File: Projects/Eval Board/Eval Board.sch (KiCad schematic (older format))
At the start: 34 parts, among them J1 Q OUT, J2 Q OUT, J3 Q OUT, J4 Q OUT, U1 LTC5584

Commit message: Version 2
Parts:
- removed J1: Q OUT, Kevin Library:SAMTEC_SMA-J-P-H-ST-EM1, symbol RandomSMAIFoundOnline:SMA-J-P-H-ST-EM1
- added J3: I Out, AdditionalLibs:SAMTEC_SMA-J-P-H-ST-EM1, symbol RandomSMAIFoundOnline:SMA-J-P-H-ST-EM1
- added J6: Conn_01x02, Connector_PinHeader_1.00mm:PinHeader_1x02_P1.00mm_Vertical, symbol Connector_Generic:Conn_01x02
- added J7: Conn_01x04, Connector_PinHeader_1.00mm:PinHeader_1x04_P1.00mm_Vertical, symbol Connector_Generic:Conn_01x04
- added J8: Conn_01x05, Connector_PinHeader_1.00mm:PinHeader_1x05_P1.00mm_Vertical, symbol Connector_Generic:Conn_01x05
- J1: renamed from J3; value Q OUT -> LO; footprint Kevin Library:SAMTEC_SMA-J-P-H-ST-EM1 -> AdditionalLibs:SAMTEC_SMA-J-P-H-ST-EM1
- J2, J4: footprint Kevin Library:SAMTEC_SMA-J-P-H-ST-EM1 -> AdditionalLibs:SAMTEC_SMA-J-P-H-ST-EM1
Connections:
- net DCOI: now also J8.4 (Pin_4)
- net DCOQ: now also J8.3 (Pin_3)
- net EDC: now also J7.2 (Pin_2)
- net EIP2: now also J7.1 (Pin_1)
- net EN: now also J7.4 (Pin_4)
- net GND: now also J6.2 (Pin_2)
- net IP2Q: now also J8.2 (Pin_2)
- net REF: now also J8.1 (Pin_1)
- net VCC: now also J6.1 (Pin_1)
- net Q-: now reaches J2.2_1, J2.2_2, J2.3_1, J2.3_2, R14.1, U1.20 (Q-)
- net Q+: now reaches J2.1, R13.1, U1.21 (Q+)
- net I+: now reaches R11.1, U1.22 (I-)
- net I+: now also J3.1
- net I-: now reaches R9.1, U1.23 (I+)
- net I-: now also J3.2_1, J3.2_2, J3.3_1, J3.3_2
- net Vbias: now reaches U1.9 (VBias)
- net Vbias: now also J7.3 (Pin_3)
- net RF: now reaches C17.1, J4.1, L6.1
- net LO: now reaches C14.1, J1.1, L5.2
- net IP2I renamed IP21
- net IP21: now also J8.5 (Pin_5)
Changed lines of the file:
@@
 Text GLabel 3100 3250 0    50   Input ~ 0
 REF
-Text GLabel 2600 3650 0    50   Input ~ 0
-IP2Q
-Text GLabel 2600 3750 0    50   Input ~ 0
-DCOQ
-Text GLabel 2600 3850 0    50   Input ~ 0
-DCOI
-Text GLabel 2600 3950 0    50   Input ~ 0
-IP2I
+$Comp
+L power:VCC #PWR0124
+U 1 1 600BE7D0
+P 5200 2350
+F 0 "#PWR0124" H 5200 2200 50  0001 C CNN
+F 1 "VCC" H 5215 2523 50  0000 C CNN
+F 2 "Connector_Pin:Pin_D0.7mm_L6.5mm_W1.8mm_FlatFork" H 5200 2350 50  0001 C CNN
+F 3 "" H 5200 2350 50  0001 C CNN
+	1    5200 2350
+	1    0    0    -1
+$EndComp
+Connection ~ 5200 2350
+Wire Wire Line
+	5200 2350 5600 2350
+$Comp
+L RandomSMAIFoundOnline:SMA-J-P-H-ST-EM1 J1
+U 1 1 600D7F64
+P 9150 4200
+F 0 "J1" H 8990 4286 50  0000 R CNN
+F 1 "LO" H 8990 4195 50  0000 R CNN
+F 2 "AdditionalLibs:SAMTEC_SMA-J-P-H-ST-EM1" H 9150 4200 50  0001 L BNN
+F 3 "" H 9150 4200 50  0001 L BNN
+F 4 "Samtec" H 9150 4200 50  0001 L BNN "MANUFACTURER"
+F 5 "G" H 9150 4200 50  0001 L BNN "PARTREV"
+F 6 "Manufacturer Recommendations" H 9150 4200 50  0001 L BNN "STANDARD"
+F 7 "3.675mm" H 9150 4200 50  0001 L BNN "MAXIMUM_PACKAGE_HEIGHT"
+	1    9150 4200
+	-1   0    0    -1
+$EndComp
 $Comp
 L RandomSMAIFoundOnline:SMA-J-P-H-ST-EM1 J2
-U 1 1 600BF77F
+U 1 1 600D2280
 P 7800 2950
 F 0 "J2" H 7640 3036 50  0000 R CNN
 F 1 "Q OUT" H 7640 2945 50  0000 R CNN
-F 2 "Kevin Library:SAMTEC_SMA-J-P-H-ST-EM1" H 7800 2950 50  0001 L BNN
+F 2 "AdditionalLibs:SAMTEC_SMA-J-P-H-ST-EM1" H 7800 2950 50  0001 L BNN
 F 3 "" H 7800 2950 50  0001 L BNN
 F 4 "Samtec" H 7800 2950 50  0001 L BNN "MANUFACTURER"
@@
 $EndComp
 $Comp
-L power:VCC #PWR0124
-U 1 1 600BE7D0
-P 5200 2350
-F 0 "#PWR0124" H 5200 2200 50  0001 C CNN
-F 1 "VCC" H 5215 2523 50  0000 C CNN
-F 2 "" H 5200 2350 50  0001 C CNN
-F 3 "" H 5200 2350 50  0001 C CNN
-	1    5200 2350
-	1    0    0    -1
-$EndComp
-Connection ~ 5200 2350
-Wire Wire Line
-	5200 2350 5600 2350
-$Comp
 L RandomSMAIFoundOnline:SMA-J-P-H-ST-EM1 J3
-U 1 1 600D7F64
-P 9150 4200
-F 0 "J3" H 8990 4286 50  0000 R CNN
-F 1 "Q OUT" H 8990 4195 50  0000 R CNN
-F 2 "Kevin Library:SAMTEC_SMA-J-P-H-ST-EM1" H 9150 4200 50  0001 L BNN
-F 3 "" H 9150 4200 50  0001 L BNN
-F 4 "Samtec" H 9150 4200 50  0001 L BNN "MANUFACTURER"
-F 5 "G" H 9150 4200 50  0001 L BNN "PARTREV"
-F 6 "Manufacturer Recommendations" H 9150 4200 50  0001 L BNN "STANDARD"
-F 7 "3.675mm" H 9150 4200 50  0001 L BNN "MAXIMUM_PACKAGE_HEIGHT"
-	1    9150 4200
-	-1   0    0    -1
-$EndComp
-$Comp
-L RandomSMAIFoundOnline:SMA-J-P-H-ST-EM1 J1
-U 1 1 600D926A
+U 1 1 600D3538
 P 2750 2950
-F 0 "J1" H 2590 3036 50  0000 R CNN
-F 1 "Q OUT" H 2590 2945 50  0000 R CNN
-F 2 "Kevin Library:SAMTEC_SMA-J-P-H-ST-EM1" H 2750 2950 50  0001 L BNN
+F 0 "J3" H 2590 3036 50  0000 R CNN
+F 1 "I Out" H 2590 2945 50  0000 R CNN
+F 2 "AdditionalLibs:SAMTEC_SMA-J-P-H-ST-EM1" H 2750 2950 50  0001 L BNN
 F 3 "" H 2750 2950 50  0001 L BNN
 F 4 "Samtec" H 2750 2950 50  0001 L BNN "MANUFACTURER"
@@
 $Comp
 L RandomSMAIFoundOnline:SMA-J-P-H-ST-EM1 J4
-U 1 1 600E48CE
+U 1 1 600D6F05
 P 2600 5050
 F 0 "J4" H 2440 5136 50  0000 R CNN
 F 1 "Q OUT" H 2440 5045 50  0000 R CNN
-F 2 "Kevin Library:SAMTEC_SMA-J-P-H-ST-EM1" H 2600 5050 50  0001 L BNN
+F 2 "AdditionalLibs:SAMTEC_SMA-J-P-H-ST-EM1" H 2600 5050 50  0001 L BNN
 F 3 "" H 2600 5050 50  0001 L BNN
 F 4 "Samtec" H 2600 5050 50  0001 L BNN "MANUFACTURER"
@@
 	1    0    0    -1
 $EndComp
+Text Label 7300 2800 0    50   ~ 0
+Q+
+Text Label 3300 2800 0    50   ~ 0
+I+
+Text Label 3300 3050 0    50   ~ 0
+I-
+Text Label 2850 4950 0    50   ~ 0
+RF
+Text Label 8950 4100 0    50   ~ 0
+LO
+Text Label 7350 3050 0    50   ~ 0
+Q-
+$Comp
+L power:VCC #PWR0125
+U 1 1 601A1C65
+P 4800 1750
+F 0 "#PWR0125" H 4800 1600 50  0001 C CNN
+F 1 "VCC" H 4815 1923 50  0000 C CNN
+F 2 "" H 4800 1750 50  0001 C CNN
+F 3 "" H 4800 1750 50  0001 C CNN
+	1    4800 1750
+	1    0    0    -1
+$EndComp
+$Comp
+L power:GND #PWR0126
+U 1 1 601A28C0
+P 4800 1850
+F 0 "#PWR0126" H 4800 1600 50  0001 C CNN
+F 1 "GND" H 4805 1677 50  0000 C CNN
+F 2 "" H 4800 1850 50  0001 C CNN
+F 3 "" H 4800 1850 50  0001 C CNN
+	1    4800 1850
+	1    0    0    -1
+$EndComp
+Text Label 2950 3650 0    50   ~ 0
+IP2Q
+Text Label 2950 3750 0    50   ~ 0
+DCOQ
+Text Label 2950 3850 0    50   ~ 0
+DCOI
+Text Label 2950 3950 0    50   ~ 0
+IP21
+Text GLabel 5400 4450 3    50   Input ~ 0
+Vbias
+Text GLabel 6800 5150 0    50   Input ~ 0
+Vbias
+Text GLabel 6800 4950 0    50   Input ~ 0
+EIP2
+Text GLabel 6800 5050 0    50   Input ~ 0
+EDC
+$Comp
+L Connector_Generic:Conn_01x02 J6
+U 1 1 601C7F3C
+P 5000 1750
+F 0 "J6" H 5080 1742 50  0000 L CNN
+F 1 "Conn_01x02" H 5080 1651 50  0000 L CNN
+F 2 "Connector_PinHeader_1.00mm:PinHeader_1x02_P1.00mm_Vertical" H 5000 1750 50  0001 C CNN
+F 3 "~" H 5000 1750 50  0001 C CNN
+	1    5000 1750
+	1    0    0    -1
+$EndComp
+$Comp
+L Connector_Generic:Conn_01x04 J7
+U 1 1 601DCEDE
+P 7000 5050
+F 0 "J7" H 7080 5042 50  0000 L CNN
+F 1 "Conn_01x04" H 7080 4951 50  0000 L CNN
+F 2 "Connector_PinHeader_1.00mm:PinHeader_1x04_P1.00mm_Vertical" H 7000 5050 50  0001 C CNN
+F 3 "~" H 7000 5050 50  0001 C CNN
+	1    7000 5050
+	1    0    0    -1
+$EndComp
+Text GLabel 6800 5250 0    50   Input ~ 0
+EN
+$Comp
+L Connector_Generic:Conn_01x05 J8
+U 1 1 601DF9CF
+P 2400 3750
+F 0 "J8" H 2318 4167 50  0000 C CNN
+F 1 "Conn_01x05" H 2318 4076 50  0000 C CNN
+F 2 "Connector_PinHeader_1.00mm:PinHeader_1x05_P1.00mm_Vertical" H 2400 3750 50  0001 C CNN
+F 3 "~" H 2400 3750 50  0001 C CNN
+	1    2400 3750
+	-1   0    0    -1
+$EndComp
+Text GLabel 2600 3550 2    50   Input ~ 0
+REF
 $EndSCHEMATC

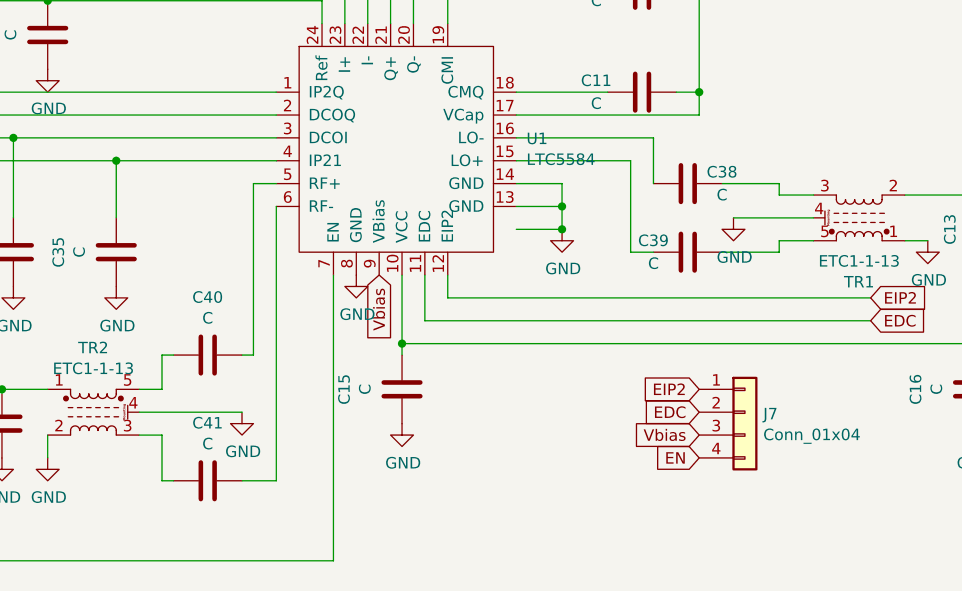
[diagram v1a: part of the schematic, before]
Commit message: adjusted trace width on I+/- and Q+/- to reduce inductance. The traces are not drawn as duplex
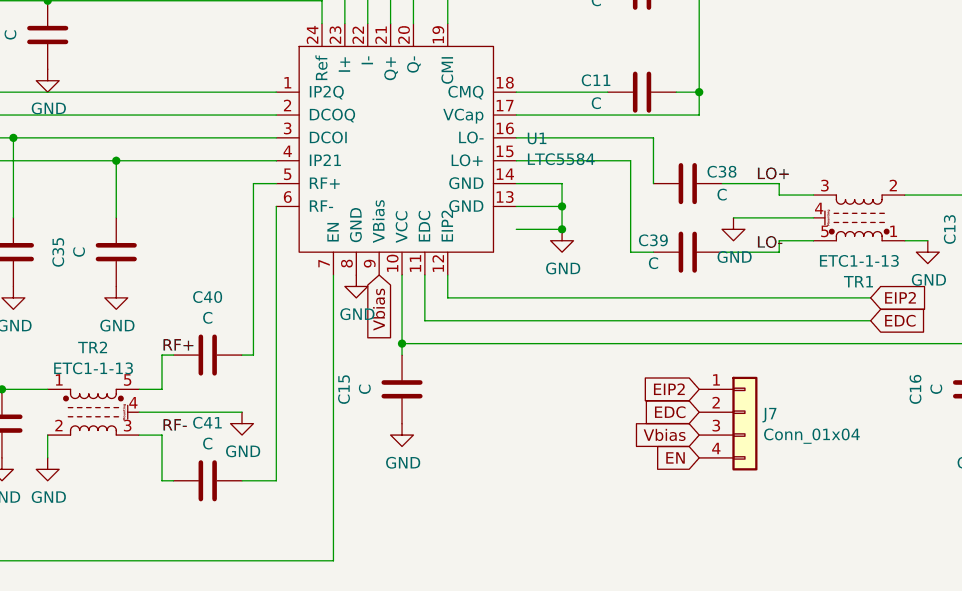
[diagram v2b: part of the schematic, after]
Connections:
- net LO+: now reaches C38.1, TR1.3
- net LO-: now reaches C39.1, TR1.5
- net RF-: now reaches C41.2, TR2.3
- net RF+: now reaches C40.2, TR2.5
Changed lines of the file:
@@
 Text GLabel 2600 3550 2    50   Input ~ 0
 REF
+Text Label 4450 4800 0    50   ~ 0
+RF+
+Text Label 4450 5150 0    50   ~ 0
+RF-
+Text Label 7050 4050 0    50   ~ 0
+LO+
+Text Label 7050 4350 0    50   ~ 0
+LO-
 $EndSCHEMATC
